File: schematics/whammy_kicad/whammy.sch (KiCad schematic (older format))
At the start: 87 parts, among them Q1 Q_NMOS_DGS, Q2 Q_PMOS_DGS, Q3 Q_NMOS_DGS, Q4 Q_PMOS_DGS, U1 Opamp_Dual_Generic, U2 L7915, U3 L7815, U4 4N35, U5 4N35

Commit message: Add footprints.
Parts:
- removed Q1, Q3: Q_NMOS_DGS, symbol Device:Q_NMOS_DGS
- removed Q2, Q4: Q_PMOS_DGS, symbol Device:Q_PMOS_DGS
- added Q1, Q3: 2SK2013, Package_TO_SOT_THT:TO-220-3_Vertical, symbol Device:Q_NMOS_GDS
- added Q2, Q4: 2SJ313, Package_TO_SOT_THT:TO-220-3_Vertical, symbol Device:Q_PMOS_GDS
- C1, C5: value C -> 1uF PP; footprint (none) -> Capacitor_THT:C_Rect_L18.0mm_W11.0mm_P15.00mm_FKS3_FKP3
- C10, C28, C3, C4, C8, C9: value CP1 -> 220uF/50V; footprint (none) -> Capacitor_THT:CP_Radial_D12.5mm_P5.00mm
- C11, C14, C15, C18, C19, C6: value CP1 -> 3300uF/35V; footprint (none) -> Capacitor_THT:CP_Radial_D18.0mm_P7.50mm
- C12, C17, C22, C25, C26, C27: value CP1 -> 22uF/25V; footprint (none) -> Capacitor_THT:CP_Radial_D6.3mm_P2.50mm
- C13, C23: value C -> 0.1uF; footprint (none) -> Capacitor_THT:C_Rect_L7.2mm_W5.5mm_P5.00mm_FKS2_FKP2_MKS2_MKP2
- C2, C7: value C -> 100pF; footprint (none) -> Capacitor_THT:C_Rect_L7.2mm_W4.5mm_P5.00mm_FKS2_FKP2_MKS2_MKP2
- C20: value C -> .22uF/250V; footprint (none) -> Capacitor_THT:C_Rect_L26.5mm_W6.0mm_P22.50mm_MKS4
- D1, D2, D3, D4, D7, D8: value D_ALT -> 1N4004; footprint (none) -> Diode_THT:D_DO-41_SOD81_P10.16mm_Horizontal
- D5, D6: value LED_ALT -> Red LED; footprint (none) -> LED_THT:LED_D3.0mm
- R1, R10, R12, R14, R2, R7: value R -> 1K; footprint (none) -> Resistor_THT:R_Axial_DIN0207_L6.3mm_D2.5mm_P10.16mm_Horizontal
- R11, R19, R26, R31: value R -> 499; footprint (none) -> Resistor_THT:R_Axial_DIN0207_L6.3mm_D2.5mm_P10.16mm_Horizontal
- R13, R9: value R -> 330; footprint (none) -> Resistor_THT:R_Axial_DIN0207_L6.3mm_D2.5mm_P10.16mm_Horizontal
- R15, R23, R24, R25, R28, R33, R34, R6: value R -> 10K; footprint (none) -> Resistor_THT:R_Axial_DIN0207_L6.3mm_D2.5mm_P10.16mm_Horizontal
- R16, R22, R29, R32: value R -> 10; footprint (none) -> Resistor_THT:R_Axial_DIN0207_L6.3mm_D2.5mm_P10.16mm_Horizontal
- R17, R27: value R -> 47; footprint (none) -> Resistor_THT:R_Axial_DIN0207_L6.3mm_D2.5mm_P10.16mm_Horizontal
- R18, R30: value R -> 100; footprint (none) -> Resistor_THT:R_Axial_DIN0207_L6.3mm_D2.5mm_P10.16mm_Horizontal
- R20, R21, R37, R38: value R -> 5R1; footprint (none) -> Resistor_THT:R_Axial_DIN0414_L11.9mm_D4.5mm_P15.24mm_Horizontal
- R3, R5: value R -> 100K; footprint (none) -> Resistor_THT:R_Axial_DIN0207_L6.3mm_D2.5mm_P10.16mm_Horizontal
- R35, R36: value R -> 47R; footprint (none) -> Resistor_THT:R_Axial_DIN0207_L6.3mm_D2.5mm_P10.16mm_Horizontal
- R39, R40: value R -> 2K2; footprint (none) -> Resistor_THT:R_Axial_DIN0207_L6.3mm_D2.5mm_P10.16mm_Horizontal
- R4, R8: value R -> 4K75; footprint (none) -> Resistor_THT:R_Axial_DIN0207_L6.3mm_D2.5mm_P10.16mm_Horizontal
- RV1: renamed from RV?; value R_POT_Dual_Separate -> 100K; footprint (none) -> WHAMMY:Potentiometer_Alps_RK271_Dual_Horizontal
- TR1: value Transformer_SP_2S -> Amveco 70053
- U1: value Opamp_Dual_Generic -> OPA2604; footprint (none) -> Package_DIP:DIP-8_W7.62mm_Socket_LongPads
- U1: renamed from U?; value Opamp_Dual_Generic -> OPA2604; footprint (none) -> Package_DIP:DIP-8_W7.62mm_Socket_LongPads
- U2, U3: footprint (none) -> Package_TO_SOT_THT:TO-220-3_Vertical
- U4, U5: footprint Package_DIP:DIP-6_W7.62mm -> Package_DIP:DIP-6_W7.62mm_Socket_LongPads
- gave numbers to parts that had none: 1
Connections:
- net +15V: now also Q1.2 (D), Q3.2 (D)
- net -15V: now also Q2.2 (D), Q4.2 (D)
- net GND: now also J1.S
- net LEFT_IN: now also J1.T
- net RIGHT_IN: now also J1.R
- net at R11.2: now also Q1.1 (G)
- net at R19.2: now also Q2.1 (G)
- net at R22.2, U4.2: now also Q2.3 (S)
- net at R16.1, R18.1: now also Q1.3 (S)
- net at R26.2: now also Q3.1 (G)
- net at R31.2: now also Q4.1 (G)
- net at R32.2, U5.2: now also Q4.3 (S)
- net at R29.1, R30.1: now also Q3.3 (S)
- no-connect marks 0 -> 2

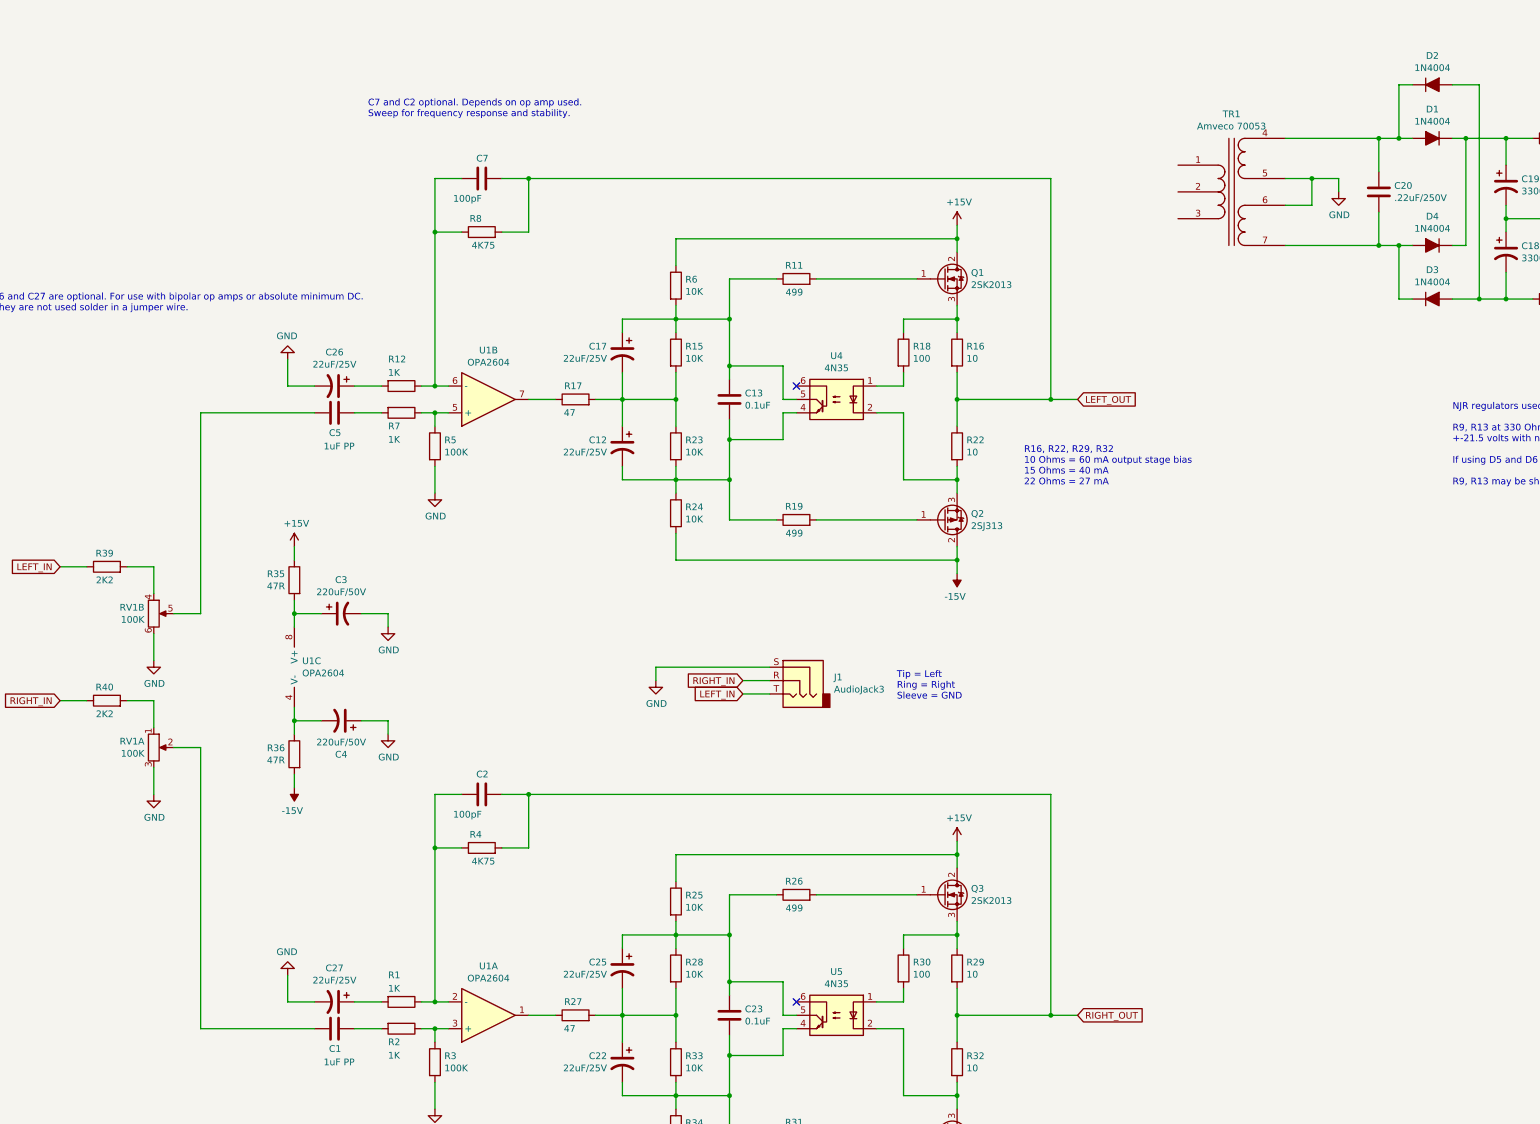
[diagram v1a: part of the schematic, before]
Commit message: First PCB version with single heatsinks.
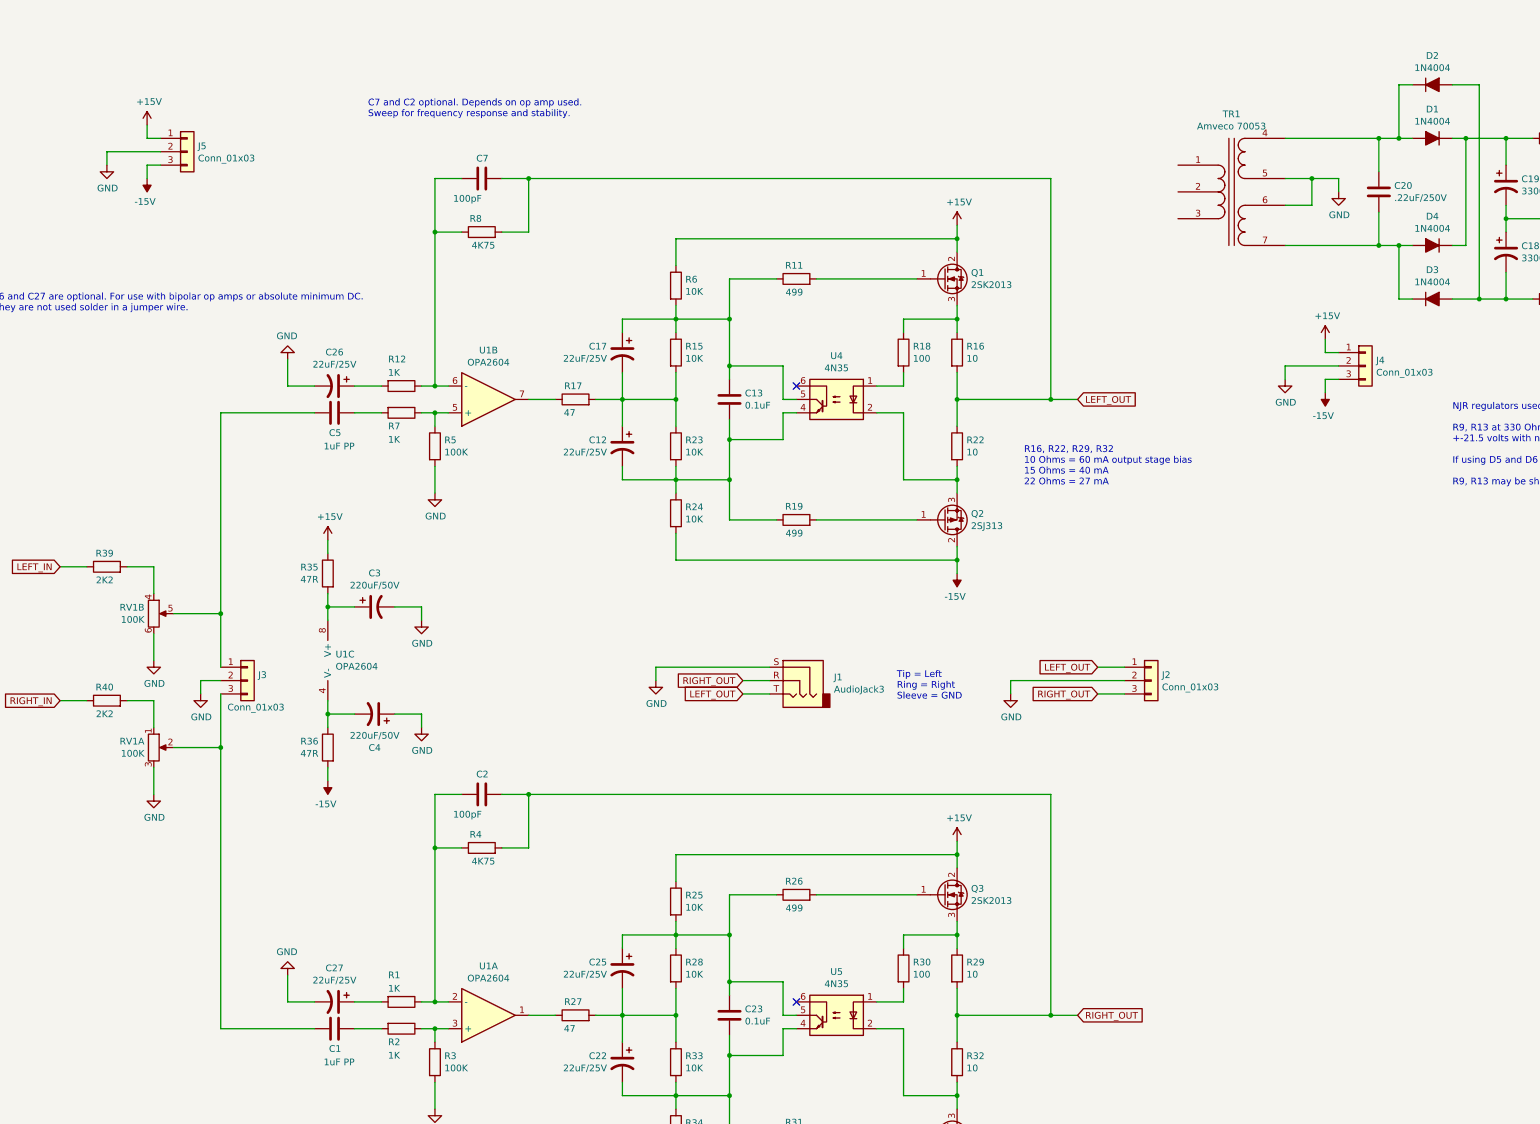
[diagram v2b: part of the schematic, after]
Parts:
- added J2, J3, J4, J5: Conn_01x03, Connector_JST:JST_EH_B3B-EH-A_1x03_P2.50mm_Vertical, symbol Connector_Generic:Conn_01x03
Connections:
- net +15V: now also J4.1 (Pin_1), J5.1 (Pin_1)
- net -15V: now also J4.3 (Pin_3), J5.3 (Pin_3)
- net GND: now also J2.2 (Pin_2), J3.2 (Pin_2), J4.2 (Pin_2), J5.2 (Pin_2)
- net LEFT_IN: no longer J1.T
- net LEFT_OUT: now also J1.T, J2.1 (Pin_1)
- net RIGHT_IN: no longer J1.R
- net RIGHT_OUT: now also J1.R, J2.3 (Pin_3)
- net at C5.1, RV1.5: now also J3.1 (Pin_1)
- net at C1.1, RV1.2: now also J3.3 (Pin_3)
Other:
- moved on the sheet: C3, C4, R35, R36, U1C

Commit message: Final version
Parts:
- added J6: Conn_Coaxial_x2, symbol Connector:Conn_Coaxial_x2
- added P1: Conn_WallPlug, symbol Connector:Conn_WallPlug
- C10, C28, C3, C4, C8, C9: value 220uF/50V -> 220uF/25V
- D1, D2, D3, D4: footprint Diode_THT:D_DO-41_SOD81_P10.16mm_Horizontal -> Diode_THT:D_DO-41_SOD81_P12.70mm_Horizontal
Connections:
- net +15V: now also J4.3 (Pin_3); no longer J4.1 (Pin_1)
- net -15V: now also J4.1 (Pin_1); no longer J4.3 (Pin_3)
- net GND: now also J6.3 (EXT)
- net LEFT_IN: now also J6.1 (IN1)
- net LEFT_OUT: now also J2.3 (Pin_3); no longer J2.1 (Pin_1)
- net RIGHT_IN: now also J6.2 (IN2)
- net RIGHT_OUT: now also J2.1 (Pin_1); no longer J2.3 (Pin_3)
- net at TR1.1 (IN+): now also P1.1 (AC_P)
- net at TR1.3 (IN-): now also P1.2 (AC_N)
- net at C5.1, RV1.5: now also J3.3 (Pin_3); no longer J3.1 (Pin_1)
- net at C1.1, RV1.2: now also J3.1 (Pin_1); no longer J3.3 (Pin_3)
- no-connect marks 2 -> 3
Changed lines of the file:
@@
 $EndComp
-Wire Wire Line
-	4150 4450 4150 4650
 Wire Wire Line
 	1850 5200 2050 5200
@@
 Wire Wire Line
 	2050 6200 2050 6400
-Wire Wire Line
-	2050 6700 2050 6900
 $Comp
 L power:GND #PWR0106
@@
 F 0 "D2" H 11600 1817 50  0000 C CNN
 F 1 "1N4004" H 11600 1726 50  0000 C CNN
-F 2 "Diode_THT:D_DO-41_SOD81_P10.16mm_Horizontal" H 11600 1600 50  0001 C CNN
+F 2 "Diode_THT:D_DO-41_SOD81_P12.70mm_Horizontal" H 11600 1600 50  0001 C CNN
 F 3 "~" H 11600 1600 50  0001 C CNN
 	1    11600 1600
@@
 F 0 "D3" H 11600 3417 50  0000 C CNN
 F 1 "1N4004" H 11600 3326 50  0000 C CNN
-F 2 "Diode_THT:D_DO-41_SOD81_P10.16mm_Horizontal" H 11600 3200 50  0001 C CNN
+F 2 "Diode_THT:D_DO-41_SOD81_P12.70mm_Horizontal" H 11600 3200 50  0001 C CNN
 F 3 "~" H 11600 3200 50  0001 C CNN
 	1    11600 3200
@@
 F 0 "D1" H 11600 2217 50  0000 C CNN
 F 1 "1N4004" H 11600 2126 50  0000 C CNN
-F 2 "Diode_THT:D_DO-41_SOD81_P10.16mm_Horizontal" H 11600 2000 50  0001 C CNN
+F 2 "Diode_THT:D_DO-41_SOD81_P12.70mm_Horizontal" H 11600 2000 50  0001 C CNN
 F 3 "~" H 11600 2000 50  0001 C CNN
 	1    11600 2000
@@
 F 0 "D4" H 11600 3017 50  0000 C CNN
 F 1 "1N4004" H 11600 2926 50  0000 C CNN
-F 2 "Diode_THT:D_DO-41_SOD81_P10.16mm_Horizontal" H 11600 2800 50  0001 C CNN
+F 2 "Diode_THT:D_DO-41_SOD81_P12.70mm_Horizontal" H 11600 2800 50  0001 C CNN
 F 3 "~" H 11600 2800 50  0001 C CNN
 	1    11600 2800
@@
 P 15050 2250
 F 0 "C10" H 15165 2296 50  0000 L CNN
-F 1 "220uF/50V" H 15150 2200 50  0000 L CNN
+F 1 "220uF/25V" H 15150 2200 50  0000 L CNN
 F 2 "Capacitor_THT:CP_Radial_D12.5mm_P5.00mm" H 15050 2250 50  0001 C CNN
 F 3 "~" H 15050 2250 50  0001 C CNN
@@
 P 15450 1750
 F 0 "C9" H 15565 1796 50  0000 L CNN
-F 1 "220uF/50V" H 15565 1705 50  0000 L CNN
+F 1 "220uF/25V" H 15565 1705 50  0000 L CNN
 F 2 "Capacitor_THT:CP_Radial_D12.5mm_P5.00mm" H 15450 1750 50  0001 C CNN
 F 3 "~" H 15450 1750 50  0001 C CNN
@@
 $EndComp
 $Comp
-L power:GND #PWR0114
-U 1 1 61749B90
-P 15050 2500
-F 0 "#PWR0114" H 15050 2250 50  0001 C CNN
-F 1 "GND" H 15055 2327 50  0000 C CNN
-F 2 "" H 15050 2500 50  0001 C CNN
-F 3 "" H 15050 2500 50  0001 C CNN
-	1    15050 2500
-	1    0    0    -1
-$EndComp
-$Comp
 L power:GND #PWR0115
 U 1 1 6174A45F
@@
 P 15050 4450
 F 0 "C8" H 15150 4400 50  0000 L CNN
-F 1 "220uF/50V" H 15150 4500 50  0000 L CNN
+F 1 "220uF/25V" H 15150 4500 50  0000 L CNN
 F 2 "Capacitor_THT:CP_Radial_D12.5mm_P5.00mm" H 15050 4450 50  0001 C CNN
 F 3 "~" H 15050 4450 50  0001 C CNN
@@
 P 15450 3950
 F 0 "C28" H 15550 3900 50  0000 L CNN
-F 1 "220uF/50V" H 15550 4000 50  0000 L CNN
+F 1 "220uF/25V" H 15550 4000 50  0000 L CNN
 F 2 "Capacitor_THT:CP_Radial_D12.5mm_P5.00mm" H 15450 3950 50  0001 C CNN
 F 3 "~" H 15450 3950 50  0001 C CNN
@@
 	14650 2500 14650 2400
 Wire Wire Line
-	15050 2500 15050 2400
-Wire Wire Line
 	15050 2100 15050 2000
 Wire Wire Line
@@
 P 3700 5500
 F 0 "C3" V 3448 5500 50  0000 C CNN
-F 1 "220uF/50V" V 3539 5500 50  0000 C CNN
+F 1 "220uF/25V" V 3539 5500 50  0000 C CNN
 F 2 "Capacitor_THT:CP_Radial_D12.5mm_P5.00mm" H 3700 5500 50  0001 C CNN
 F 3 "~" H 3700 5500 50  0001 C CNN
@@
 P 3700 6300
 F 0 "C4" V 3448 6300 50  0000 C CNN
-F 1 "220uF/50V" V 3539 6300 50  0000 C CNN
+F 1 "220uF/25V" V 3539 6300 50  0000 C CNN
 F 2 "Capacitor_THT:CP_Radial_D12.5mm_P5.00mm" H 3700 6300 50  0001 C CNN
 F 3 "~" H 3700 6300 50  0001 C CNN
@@
 F 3 "~" H 9500 6050 50  0001 C CNN
 	1    9500 6050
-	1    0    0    -1
+	1    0    0    1
 $EndComp
 Text GLabel 9100 5950 0    50   Input ~ 0
@@
 F 3 "~" H 2750 6050 50  0001 C CNN
 	1    2750 6050
-	1    0    0    -1
+	1    0    0    1
 $EndComp
 $Comp
@@
 F 3 "~" H 11100 3700 50  0001 C CNN
 	1    11100 3700
-	1    0    0    -1
+	1    0    0    1
 $EndComp
 $Comp
@@
 	2550 6150 2550 6550
 Connection ~ 2550 6550
+$Comp
+L Connector:Conn_Coaxial_x2 J6
+U 1 1 61705347
+P 5050 5450
+F 0 "J6" H 5150 5425 50  0000 L CNN
+F 1 "Conn_Coaxial_x2" H 5150 5334 50  0000 L CNN
+F 2 "" H 5050 5350 50  0001 C CNN
+F 3 " ~" H 5050 5350 50  0001 C CNN
+	1    5050 5450
+	1    0    0    -1
+$EndComp
+$Comp
+L power:GND #PWR0136
+U 1 1 6170F30C
+P 5050 5850
+F 0 "#PWR0136" H 5050 5600 50  0001 C CNN
+F 1 "GND" H 5055 5677 50  0000 C CNN
+F 2 "" H 5050 5850 50  0001 C CNN
+F 3 "" H 5050 5850 50  0001 C CNN
+	1    5050 5850
+	1    0    0    -1
+$EndComp
+Text GLabel 4750 5350 0    50   Input ~ 0
+LEFT_IN
+Text GLabel 4750 5550 0    50   Input ~ 0
+RIGHT_IN
+Wire Wire Line
+	5050 5750 5050 5850
+Wire Wire Line
+	4750 5350 4850 5350
+Wire Wire Line
+	4750 5550 4850 5550
+Wire Wire Line
+	2050 6700 2050 6900
+Wire Wire Line
+	4150 4450 4150 4650
+$Comp
+L power:GND #PWR0114
+U 1 1 618865DE
+P 15050 2500
+F 0 "#PWR0114" H 15050 2250 50  0001 C CNN
+F 1 "GND" H 15055 2327 50  0000 C CNN
+F 2 "" H 15050 2500 50  0001 C CNN
+F 3 "" H 15050 2500 50  0001 C CNN
+	1    15050 2500
+	1    0    0    -1
+$EndComp
+Wire Wire Line
+	15050 2500 15050 2400
+$Comp
+L Connector:Conn_WallPlug P1
+U 1 1 618AA4D6
+P 9350 2400
+F 0 "P1" H 9367 2725 50  0000 C CNN
+F 1 "Conn_WallPlug" H 9367 2634 50  0000 C CNN
+F 2 "" H 9750 2400 50  0001 C CNN
+F 3 "~" H 9750 2400 50  0001 C CNN
+	1    9350 2400
+	1    0    0    -1
+$EndComp
+Wire Wire Line
+	9550 2300 9550 2200
+Wire Wire Line
+	9550 2200 9700 2200
+Wire Wire Line
+	9550 2500 9550 2600
+Wire Wire Line
+	9550 2600 9700 2600
+NoConn ~ 9700 2400
 $EndSCHEMATC
